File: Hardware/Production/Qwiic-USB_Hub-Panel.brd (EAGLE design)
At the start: 43.2 x 81.3 mm, 98 parts, among them J1 USB_A_FEMALE, J2 Qwiic Right Angle, J3 PTH, J4 Qwiic Right Angle, J6 USB_A_FEMALE, J8 USB_A_FEMALE, J9 USB_A_FEMALE, Q1 4.3A/20V/54mΩ, Q2 4.3A/20V/54mΩ, Q3 4.3A/20V/54mΩ, Q4 4.3A/20V/54mΩ, U1 USB251XB, U2 3.3V, Y1 24MHz

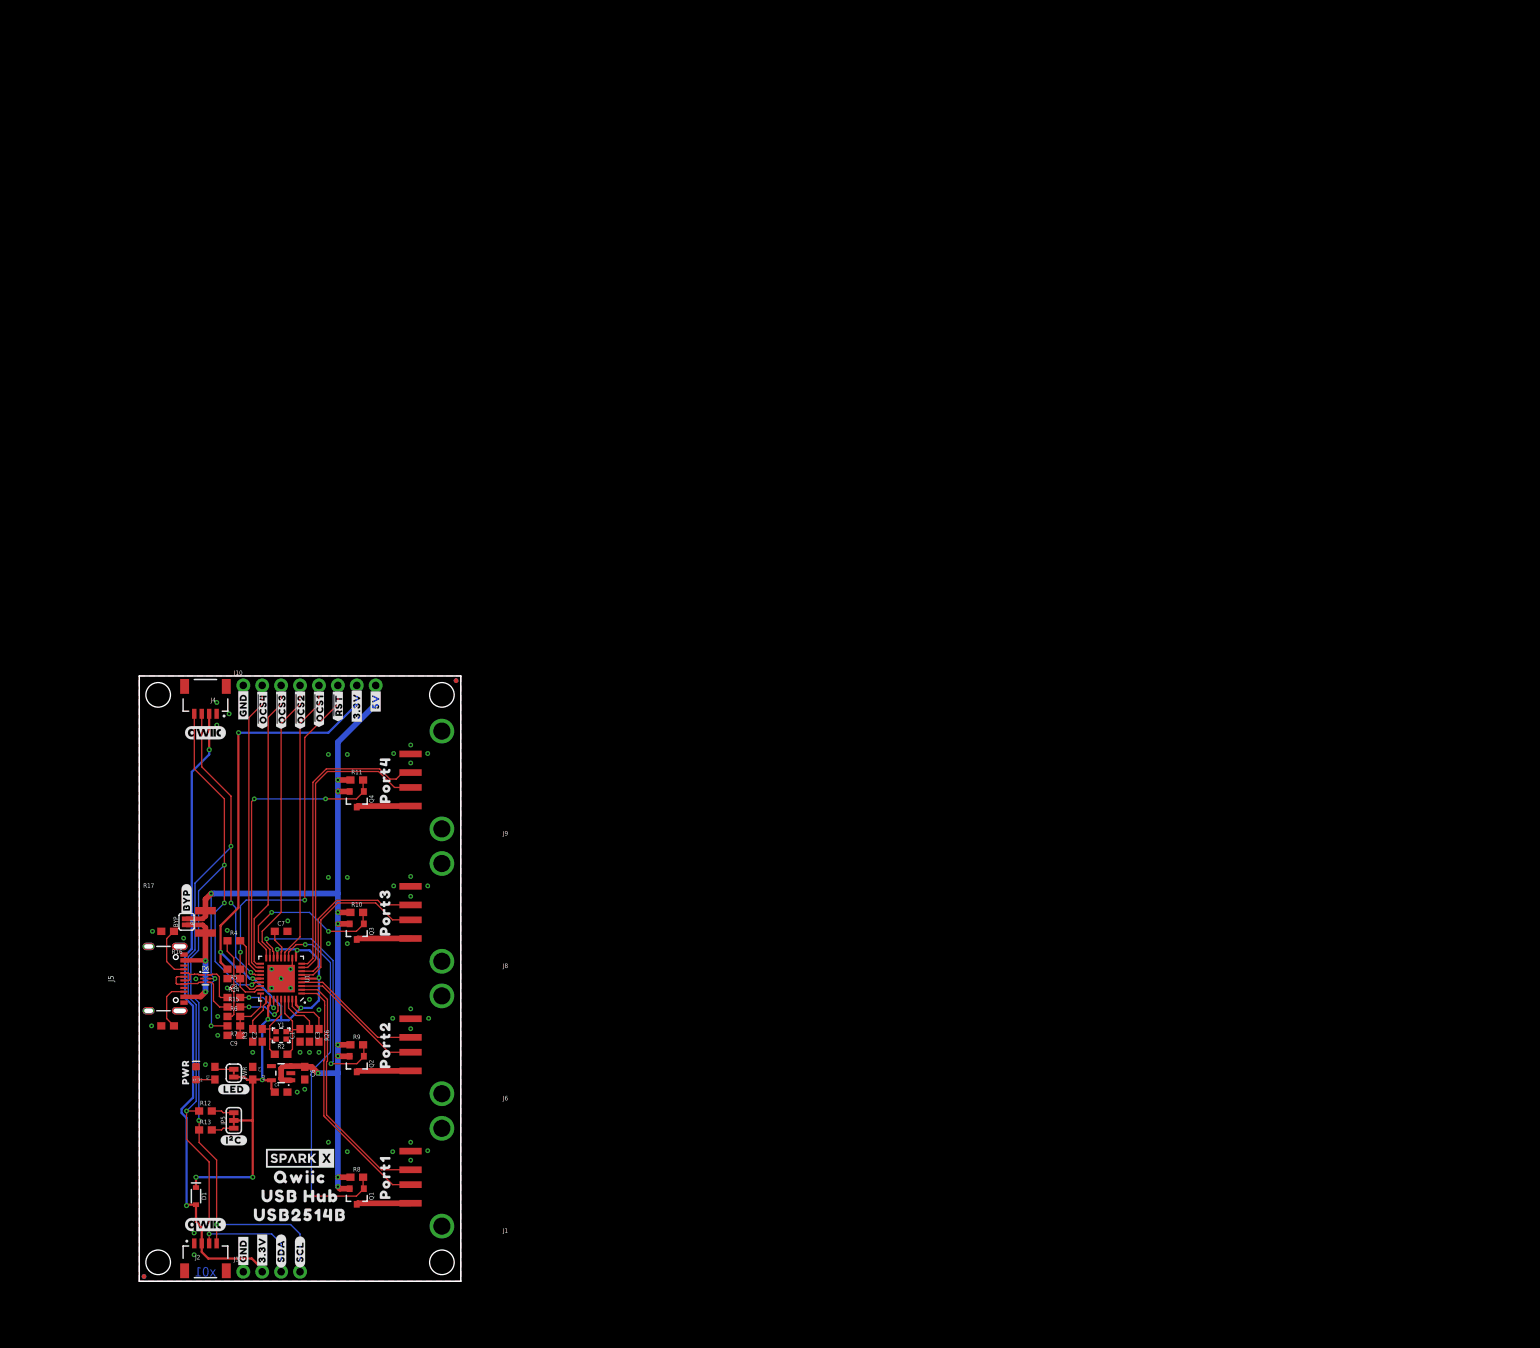
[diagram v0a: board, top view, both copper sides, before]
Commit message: Fixing silk typo in OCS labels. Adding production panels.
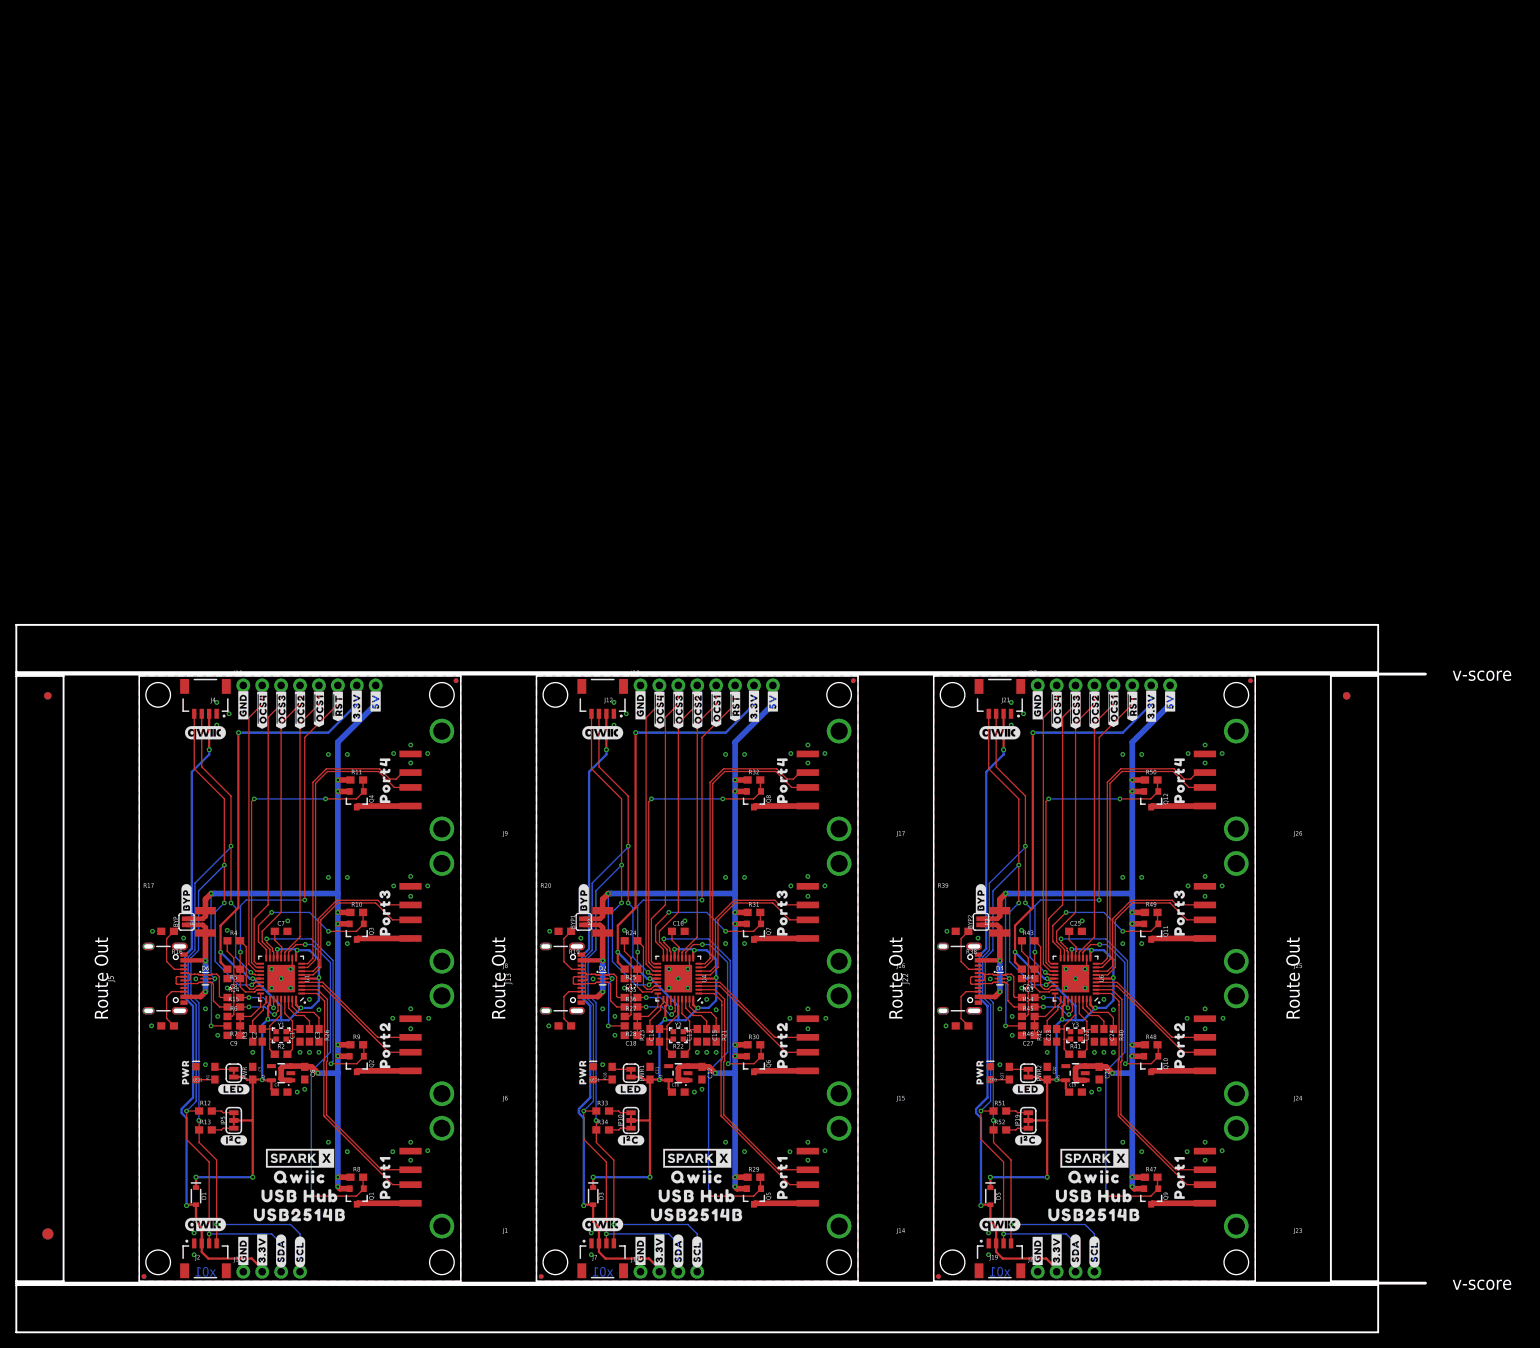
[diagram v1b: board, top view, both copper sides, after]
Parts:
- removed FRAME2: FRAME-LEDGER, SparkFun-Aesthetics:CREATIVE_COMMONS
- added BYP1, BYP2: JUMPER-SMT_2_NO_SILK, SparkFun-Jumpers:SMT-JUMPER_2_NO_SILK
- added C10, C12, C19, C21: 1.0uF, SparkFun-Capacitors:0603
- added C11, C15, C16, C17, C18, C20, C24, C25, C26, C27: 0.1uF, SparkFun-Capacitors:0603
- added C13, C14, C22, C23: 18pF, SparkFun-Capacitors:0603
- added D2, D4: PRTR5V0U2F, SparkFun-IC-Power:SOT886
- added D3, D5: 3A/10V/280mV, SparkFun-DiscreteSemi:SOD-323
- added E$1, E$2, E$3, E$4: (no value), SparkFun-Aesthetics:FIDUCIAL-1X2
- added E$5, E$6: (no value), SparkFun-Retired:FIDUCIAL-1.5X3
- added F2, F3: 6V/2A, SparkFun-Fuses:1210
- added J11, J20: PTH, SparkX:1X04_NO_SILK
- added J12, J19, J21, J7: Qwiic Right Angle, SparkFun-Connectors:JST04_1MM_RA
- added J13, J22: (no value), SparkFun-Connectors:USB-C-16P-2LAYER-PADS
- added J14, J15, J16, J17, J23, J24, J25, J26: USB_A_FEMALE, SparkFun-Connectors:USB-A-S-NOSILK-FEMALE
- added J18, J27: (no value), SparkFun-Connectors:1X08_NO_SILK
- added JP1, JP11, JP12, JP17, JP18, JP2, JP8, JP9: STAND-OFF, SparkFun:STAND-OFF
- added JP10, JP19: (no value), SparkFun-Jumpers:SMT-JUMPER_3_2-NC_TRACE_SILK
- added JP13, JP14, JP15, JP16, JP3, JP4, JP6, JP7: FIDUCIALUFIDUCIAL, SparkFun:MICRO-FIDUCIAL
- added LED1, LED3: RED, SparkFun-LED:LED-0603
- added LOGO3, LOGO5: OSHW-LOGOMINI, SparkFun-Aesthetics:OSHW-LOGO-MINI
- added LOGO4, LOGO6: QWIIC_LOGO_CONNECTOR, SparkFun-Aesthetics:QWIIC_5.5MM
- added PWR1, PWR2: (no value), SparkFun-Jumpers:SMT-JUMPER_2_NC_TRACE_SILK
- added Q10, Q11, Q12, Q5, Q6, Q7, Q8, Q9: 4.3A/20V/54mΩ, SparkFun-DiscreteSemi:SOT23-3
- added R18, R37: 1k, SparkFun-Resistors:0603
- added R19, R20, R38, R39: 5.1k, SparkFun-Resistors:0603
- added R21, R40: 12k, SparkFun-Resistors:0603
- added R22, R41: 1M, SparkFun-Resistors:0603
- added R23, R24, R25, R27, R28, R29, R30, R31, R32, R42, R43, R44, R45, R46, R47, R48, R49, R50: 100k, SparkFun-Resistors:0603
- added R33, R34, R51, R52: 2.2k, SparkFun-Resistors:0603
- added R35, R36, R53, R54: 22, SparkFun-Resistors:0603
- added U$100, U$53, U$63, U$90: (no value), output:##RST##4
- added U$101, U$54, U$64, U$91: (no value), output:#3#3V#6
- added U$102, U$55, U$65, U$92: (no value), output:#5V#7
- added U$103, U$30, U$66, U$79: SPARKX-LOGO4, SparkX:SPARKX-MEDIUM
- added U$104, U$59, U$67, U$96: (no value), output:QWIIC2
- added U$105, U$60, U$68, U$97: (no value), output:USB_HUB1
- added U$106, U$58, U$69, U$95: (no value), output:USB2514B0
- added U$107, U$70: (no value), SparkFun-Aesthetics:QWIIC_5.5MM
- added U$108, U$71: (no value), output:##OCS1##3
- added U$109, U$72: (no value), output:##OCS2##2
- added U$110, U$73: (no value), output:##OCS3##1
- added U$111, U$74: (no value), output:##OCS4##0
- added U$24, U$75: (no value), output:PORT40
- added U$25, U$76: (no value), output:PORT31
- added U$28, U$77: (no value), output:PORT22
- added U$29, U$78: (no value), output:PORT13
- added U$43, U$46, U$80, U$83: (no value), output:#3#3V#0
- added U$44, U$47, U$81, U$84: (no value), output:#SDA#0
- added U$45, U$48, U$82, U$85: (no value), output:#SCL#0
- added U$49, U$50, U$86, U$87: (no value), output:#GND#0
- added U$51, U$88: (no value), output:#I�C#1
- added U$52, U$89: (no value), output:PWR0
- added U$56, U$62, U$93, U$99: (no value), output:#GND#5
- added U$57, U$94: (no value), output:#BYP#0
- added U$61, U$98: (no value), output:#LED#0
- added U3, U5: 3.3V, SparkFun-IC-Power:SOT23-5
- added U4, U6: USB251XB, USB251xB:QFN-36
- added Y2, Y3: 24MHz, SparkFun-Clocks:CRYSTAL-SMD-2.0X1.6MM
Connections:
- new net !OCS10: J27.4, U6.17
- new net !OCS11: J27.3, U6.19
- new net !OCS12: J27.2, U6.21
- new net !OCS5: J18.5, U4.13
- new net !OCS6: J18.4, U4.17
- new net !OCS7: J18.3, U4.19
- new net !OCS8: J18.2, U4.21
- new net !OCS9: J27.5, U6.13
- new net !RESET1: C17.1, J18.6, R25.1, U4.26
- new net !RESET2: C26.1, J27.6, R44.1, U6.26
- new net 3.3V1: C10.1, C11.2, D3.C, J18.7, JP10.2, PWR1.2, R25.2, U3.5, U4.10, U4.15, U4.23, U4.29, U4.36, U4.5
- new net 3.3V2: C19.1, C20.2, D5.C, J27.7, JP19.2, PWR2.2, R44.2, U5.5, U6.10, U6.15, U6.23, U6.29, U6.36, U6.5
- new net 5V1: BYP1.2, C12.1, D2.5, F2.2, J18.8, Q5.2, Q6.2, Q7.2, Q8.2, R28.2, R29.1, R30.1, R31.1, R32.1, U3.1, U3.3
- new net 5V2: BYP2.2, C21.1, D4.5, F3.2, J27.8, Q10.2, Q11.2, Q12.2, Q9.2, R46.2, R47.1, R48.1, R49.1, R50.1, U5.1, U5.3
- new net CC3: J13.A5, R20.2
- new net CC4: J13.B5, R19.2
- new net CC5: J22.A5, R39.2
- new net CC6: J22.B5, R38.2
- new net D_N1: D2.6, R35.1
- new net D_N2: D4.6, R53.1
- new net D_P1: D2.4, R36.1
- new net D_P2: D4.4, R54.1
- new net GND1: C10.2, C11.1, C12.2, C13.1, C14.1, C15.2, C16.2, C17.2, C18.2, D2.2, J11.1, J12.1, J13.GND, J13.GND2, J13.SHLD1, J13.SHLD2, J13.SHLD3, J13.SHLD4, J14.GND, J15.GND, J16.GND, J17.GND, J18.1, J7.1, LED1.C, R19.1, R20.1, R21.2, R23.1, R24.1, R27.1, U3.2, U4.11, U4.EP
- new net GND2: C19.2, C20.1, C21.2, C22.1, C23.1, C24.2, C25.2, C26.2, C27.2, D4.2, J19.1, J20.1, J21.1, J22.GND, J22.GND2, J22.SHLD1, J22.SHLD2, J22.SHLD3, J22.SHLD4, J23.GND, J24.GND, J25.GND, J26.GND, J27.1, LED3.C, R38.1, R39.1, R40.2, R42.1, R43.1, R45.1, U5.2, U6.11, U6.EP
- new net N$19: LED1.A, R18.1
- new net N$20: PWR1.1, R18.2
- new net N$22: C13.2, R22.2, U4.33, Y2.3
- new net N$23: C14.2, R22.1, U4.32, Y2.1
- new net N$24: R21.1, U4.35
- new net N$25: R23.2, U4.28
- new net N$26: R24.2, U4.25
- new net N$27: C15.1, U4.34
- new net N$28: C16.1, U4.14
- new net N$29: J14.VBUS, Q5.3
- new net N$30: J15.VBUS, Q6.3
- new net N$31: J16.VBUS, Q7.3
- new net N$32: J17.VBUS, Q8.3
- new net N$33: BYP1.1, F2.1, J13.VBUS1, J13.VBUS2
- new net N$34: JP10.1, R34.2
- new net N$35: JP10.3, R33.2
- new net N$36: R35.2, U4.30
- new net N$37: R36.2, U4.31
- new net N$38: D3.A, J11.2, J12.2, J7.2
- new net N$39: LED3.A, R37.1
- new net N$40: PWR2.1, R37.2
- new net N$41: C22.2, R41.2, U6.33, Y3.3
- new net N$42: C23.2, R41.1, U6.32, Y3.1
- new net N$43: R40.1, U6.35
- new net N$44: R42.2, U6.28
- new net N$45: R43.2, U6.25
- new net N$46: C24.1, U6.34
- new net N$47: C25.1, U6.14
- new net N$48: J23.VBUS, Q9.3
- new net N$49: J24.VBUS, Q10.3
- new net N$50: J25.VBUS, Q11.3
- new net N$51: J26.VBUS, Q12.3
- new net N$52: BYP2.1, F3.1, J22.VBUS1, J22.VBUS2
- new net N$53: JP19.1, R52.2
- new net N$54: JP19.3, R51.2
- new net N$55: R53.2, U6.30
- new net N$56: R54.2, U6.31
- new net N$57: D5.A, J19.2, J20.2, J21.2
- new net PORT1_N1: J14.D-, U4.1
- new net PORT1_N2: J23.D-, U6.1
- new net PORT1_P1: J14.D+, U4.2
- new net PORT1_P2: J23.D+, U6.2
- new net PORT2_N1: J15.D-, U4.3
- new net PORT2_N2: J24.D-, U6.3
- new net PORT2_P1: J15.D+, U4.4
- new net PORT2_P2: J24.D+, U6.4
- new net PORT3_N1: J16.D-, U4.6
- new net PORT3_N2: J25.D-, U6.6
- new net PORT3_P1: J16.D+, U4.7
- new net PORT3_P2: J25.D+, U6.7
- new net PORT4_N1: J17.D-, U4.8
- new net PORT4_N2: J26.D-, U6.8
- new net PORT4_P1: J17.D+, U4.9
- new net PORT4_P2: J26.D+, U6.9
- new net PRTPWR10: Q10.1, R48.2, U6.16
- new net PRTPWR11: Q11.1, R49.2, U6.18
- new net PRTPWR12: Q12.1, R50.2, U6.20
- new net PRTPWR5: Q5.1, R29.2, U4.12
- new net PRTPWR6: Q6.1, R30.2, U4.16
- new net PRTPWR7: Q7.1, R31.2, U4.18
- new net PRTPWR8: Q8.1, R32.2, U4.20
- new net PRTPWR9: Q9.1, R47.2, U6.12
- new net SCL1: J11.4, J12.4, J7.4, R34.1, U4.24
- new net SCL2: J19.4, J20.4, J21.4, R52.1, U6.24
- new net SDA1: J11.3, J12.3, J7.3, R33.1, U4.22
- new net SDA2: J19.3, J20.3, J21.3, R51.1, U6.22
- new net UNP_D+1: D2.3, J13.A6, J13.B6
- new net UNP_D+2: D4.3, J22.A6, J22.B6
- new net UNP_D-1: D2.1, J13.A7, J13.B7
- new net UNP_D-2: D4.1, J22.A7, J22.B7
- new net VBUS_DET1: C18.1, R27.2, R28.1, U4.27
- new net VBUS_DET2: C27.1, R45.2, R46.1, U6.27
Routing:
- net 5V2: track 0.00 -> 138.1 mm, vias 0 -> 12
- net 5V1: track 0.00 -> 138.1 mm, vias 0 -> 12
- net 3.3V2: track 0.00 -> 136.2 mm, vias 0 -> 11
- net 3.3V1: track 0.00 -> 136.2 mm, vias 0 -> 11
- net SCL2: track 0.00 -> 113.9 mm, vias 0 -> 5
- net SCL1: track 0.00 -> 113.9 mm, vias 0 -> 5
- net SDA2: track 0.00 -> 112.6 mm, vias 0 -> 5
- net SDA1: track 0.00 -> 112.6 mm, vias 0 -> 5
- net N$57: track 0.00 -> 86.2 mm, vias 0 -> 2
- net N$38: track 0.00 -> 86.2 mm, vias 0 -> 2
- net !RESET1: track 0.00 -> 53.7 mm, vias 0 -> 2
- net !RESET2: track 0.00 -> 53.7 mm, vias 0 -> 2
- net PRTPWR5: track 0.00 -> 49.3 mm, vias 0 -> 2
- net PRTPWR9: track 0.00 -> 49.3 mm, vias 0 -> 2
- net PRTPWR8: track 0.00 -> 40.3 mm, vias 0 -> 2
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- added copper zone on layer 1, net GND1
- added copper zone on layer 16, net GND1
- added copper zone on layer 1, net GND2
- added copper zone on layer 16, net GND2
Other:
- board size 43.2 x 81.3 mm -> 189.2 x 95 mm
- board text added: "Route Out"
- board text added: "v-score"
- board text removed: "Measurements in inches"

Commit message: Panel for x02
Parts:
- added U$112, U$120: (no value), output:QWIIC2
- added U$113, U$121: (no value), output:USB_HUB1
- added U$114: (no value), output:#LED#0
- added U$115: (no value), output:#GND#5
- added U$116: (no value), output:##RST##4
- added U$117: (no value), output:#3#3V#6
- added U$118: (no value), output:#5V#7
- added U$119: SPARKX-LOGO4, SparkX:SPARKX-MEDIUM
- added U$122: (no value), output:USB2514B0
- added U$123: (no value), SparkFun-Aesthetics:QWIIC_5.5MM
- added U$124, U$132: (no value), output:##OCS1##3
- added U$125, U$133: (no value), output:##OCS2##2
- added U$126, U$134: (no value), output:##OCS3##1
- added U$127, U$135: (no value), output:##OCS4##0
- added U$128, U$131: (no value), output:#CFG0#1
- added U$129, U$130: (no value), output:#CFG1#0
- J10, J18, J27: device SparkFun-Connectors:1X08_NO_SILK -> SparkFun-Connectors:1X10_NO_SILK
- JP10, JP19, JP5: device SparkFun-Jumpers:SMT-JUMPER_3_2-NC_TRACE_SILK -> SparkFun-Jumpers:SMT-JUMPER_3_NO_SILK
- U$100: device output:##RST##4 -> output:#SDA#0
- U$101: device output:#3#3V#6 -> output:#SCL#0
- U$102: device output:#5V#7 -> output:#GND#0
- U$103: value SPARKX-LOGO4 -> (none); device SparkX:SPARKX-MEDIUM -> output:#GND#0
- U$104, U$59: device output:QWIIC2 -> output:#I�C#1
- U$105, U$60: device output:USB_HUB1 -> output:PWR0
- U$106: device output:USB2514B0 -> output:##RST##4
- U$107: device SparkFun-Aesthetics:QWIIC_5.5MM -> output:#3#3V#6
- U$108: device output:##OCS1##3 -> output:#5V#7
- U$109: device output:##OCS2##2 -> output:#GND#5
- U$110: device output:##OCS3##1 -> output:#BYP#0
- U$111: device output:##OCS4##0 -> output:USB2514B0
- U$24: device output:PORT40 -> output:#CFG0#1
- U$25: device output:PORT31 -> output:#CFG1#0
- U$28: device output:PORT22 -> output:#CFG1#0
- U$29: device output:PORT13 -> output:#CFG0#1
- U$30, U$79: value SPARKX-LOGO4 -> (none); device SparkX:SPARKX-MEDIUM -> output:##OCS1##3
- U$43, U$80: device output:#3#3V#0 -> output:##OCS2##2
- U$44, U$81: device output:#SDA#0 -> output:##OCS3##1
- U$45, U$82: device output:#SCL#0 -> output:##OCS4##0
- U$46: device output:#3#3V#0 -> output:PORT40
- U$47: device output:#SDA#0 -> output:PORT31
- U$48: device output:#SCL#0 -> output:PORT22
- U$49: device output:#GND#0 -> output:PORT13
- U$50: value (none) -> SPARKX-LOGO4; device output:#GND#0 -> SparkX:SPARKX-MEDIUM
- U$51: device output:#I�C#1 -> output:#3#3V#0
- U$52: device output:PWR0 -> output:#SDA#0
- U$53: device output:##RST##4 -> output:#SCL#0
- U$54: device output:#3#3V#6 -> output:#3#3V#0
- U$55: device output:#5V#7 -> output:#SDA#0
- U$56: device output:#GND#5 -> output:#SCL#0
- U$57: device output:#BYP#0 -> output:#GND#0
- U$58: device output:USB2514B0 -> output:#GND#0
- U$61: device output:#LED#0 -> output:##RST##4
- U$62: device output:#GND#5 -> output:#3#3V#6
- U$63: device output:##RST##4 -> output:#5V#7
- U$64: device output:#3#3V#6 -> output:#GND#5
- U$65: device output:#5V#7 -> output:#BYP#0
- U$66: value SPARKX-LOGO4 -> (none); device SparkX:SPARKX-MEDIUM -> output:USB2514B0
- U$69: device output:USB2514B0 -> output:#LED#0
- U$70: device SparkFun-Aesthetics:QWIIC_5.5MM -> output:#GND#5
- U$71: device output:##OCS1##3 -> output:##RST##4
- U$72: device output:##OCS2##2 -> output:#3#3V#6
- U$73: device output:##OCS3##1 -> output:#5V#7
- U$74: value (none) -> SPARKX-LOGO4; device output:##OCS4##0 -> SparkX:SPARKX-MEDIUM
- U$75: device output:PORT40 -> output:QWIIC2
- U$76: device output:PORT31 -> output:USB_HUB1
- U$77: device output:PORT22 -> output:USB2514B0
- U$78: device output:PORT13 -> SparkFun-Aesthetics:QWIIC_5.5MM
- U$83: device output:#3#3V#0 -> output:#CFG0#1
- U$84: device output:#SDA#0 -> output:#CFG1#0
- U$85: device output:#SCL#0 -> output:#CFG1#0
- U$86: device output:#GND#0 -> output:#CFG0#1
- U$87: device output:#GND#0 -> output:##OCS1##3
- U$88: device output:#I�C#1 -> output:##OCS2##2
- U$89: device output:PWR0 -> output:##OCS3##1
- U$90: device output:##RST##4 -> output:##OCS4##0
- U$91: device output:#3#3V#6 -> output:PORT40
- U$92: device output:#5V#7 -> output:PORT31
- U$93: device output:#GND#5 -> output:PORT22
- U$94: device output:#BYP#0 -> output:PORT13
- U$95: value (none) -> SPARKX-LOGO4; device output:USB2514B0 -> SparkX:SPARKX-MEDIUM
- U$96: device output:QWIIC2 -> output:#3#3V#0
- U$97: device output:USB_HUB1 -> output:#SDA#0
- U$98: device output:#LED#0 -> output:#SCL#0
- U$99: device output:#GND#5 -> output:#3#3V#0
- moved U$82 93.4 mm to (69.8, 76.8)
- moved U$45 93.4 mm to (16.5, 76.8), flipped to the bottom
- moved U$44 90.2 mm to (19.1, 76.8), flipped to the bottom
- moved U$81 90.2 mm to (72.4, 76.8)
- moved U$43 87.2 mm to (21.6, 76.8), flipped to the bottom
- moved U$80 87.2 mm to (74.9, 76.8)
- moved U$85 86.3 mm to (82.5, 77.1)
- moved U$84 84.8 mm to (82.5, 77.1), flipped to the top
- moved U$87 84.7 mm to (77.5, 77.0)
- moved U$75 83.9 mm to (74.9, 14.0), flipped to the bottom, turned to 0 degrees
- moved U$29 83.4 mm to (31.8, 77.0), flipped to the bottom
- moved U$83 82.1 mm to (85.1, 77.0), flipped to the top
- moved U$86 81.1 mm to (85.1, 77.0), flipped to the bottom
- moved U$30 79.0 mm to (24.1, 77.0), flipped to the bottom, turned to 90 degrees
- moved U$79 79.0 mm to (77.5, 77.0), turned to 90 degrees
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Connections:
- removed net N$12 (its old number): R4.2, U1.25
- removed net N$26 (its old number): R24.2, U4.25
- removed net N$45 (its old number): R43.2, U6.25
- removed net SCL: J2.4, J3.4, J4.4, R13.1, U1.24
- removed net SCL1: J11.4, J12.4, J7.4, R34.1, U4.24
- removed net SCL2: J19.4, J20.4, J21.4, R52.1, U6.24
- new net CFG1: J10.7, R4.2, U1.25
- new net CFG2: J18.7, R24.2, U4.25
- new net CFG3: J27.7, R43.2, U6.25
- new net SCL/CFG0: J10.8, J2.4, J3.4, J4.4, R13.1, U1.24
- new net SCL/CFG1: J11.4, J12.4, J18.8, J7.4, R34.1, U4.24
- new net SCL/CFG2: J19.4, J20.4, J21.4, J27.8, R52.1, U6.24
- net 3.3V: now also J10.9; no longer J10.7
- net 3.3V1: now also J18.9; no longer J18.7
- net 3.3V2: now also J27.9; no longer J27.7
- net 5V: now also J10.10; no longer J10.8
- net 5V1: now also J18.10; no longer J18.8
- net 5V2: now also J27.10; no longer J27.8
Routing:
- net SCL/CFG2: track 0.00 -> 143.6 mm, vias 0 -> 7
- net SCL/CFG1: track 0.00 -> 143.6 mm, vias 0 -> 7
- net SCL/CFG0: track 0.00 -> 143.6 mm, vias 0 -> 7
- net SCL2: track 113.9 -> 0.00 mm, vias 5 -> 0
- net SCL1: track 113.9 -> 0.00 mm, vias 5 -> 0
- net SCL: track 113.9 -> 0.00 mm, vias 5 -> 0
- net CFG2: track 0.00 -> 56.1 mm, vias 0 -> 2
- net CFG1: track 0.00 -> 56.1 mm, vias 0 -> 2
- net CFG3: track 0.00 -> 56.1 mm, vias 0 -> 2
- net N$45 (its old number): track 8.67 -> 0.00 mm
- net N$26 (its old number): track 8.67 -> 0.00 mm
- net N$12 (its old number): track 8.67 -> 0.00 mm
- net 3.3V2: track 136.2 -> 139.8 mm
- net 3.3V1: track 136.2 -> 139.8 mm
- net 3.3V: track 136.2 -> 139.8 mm
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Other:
- board text added: "x02"
- board text removed: "x01"
